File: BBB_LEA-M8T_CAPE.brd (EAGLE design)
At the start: 54.6 x 71.8 mm, 36 parts, among them U2 MIC5225-3.3

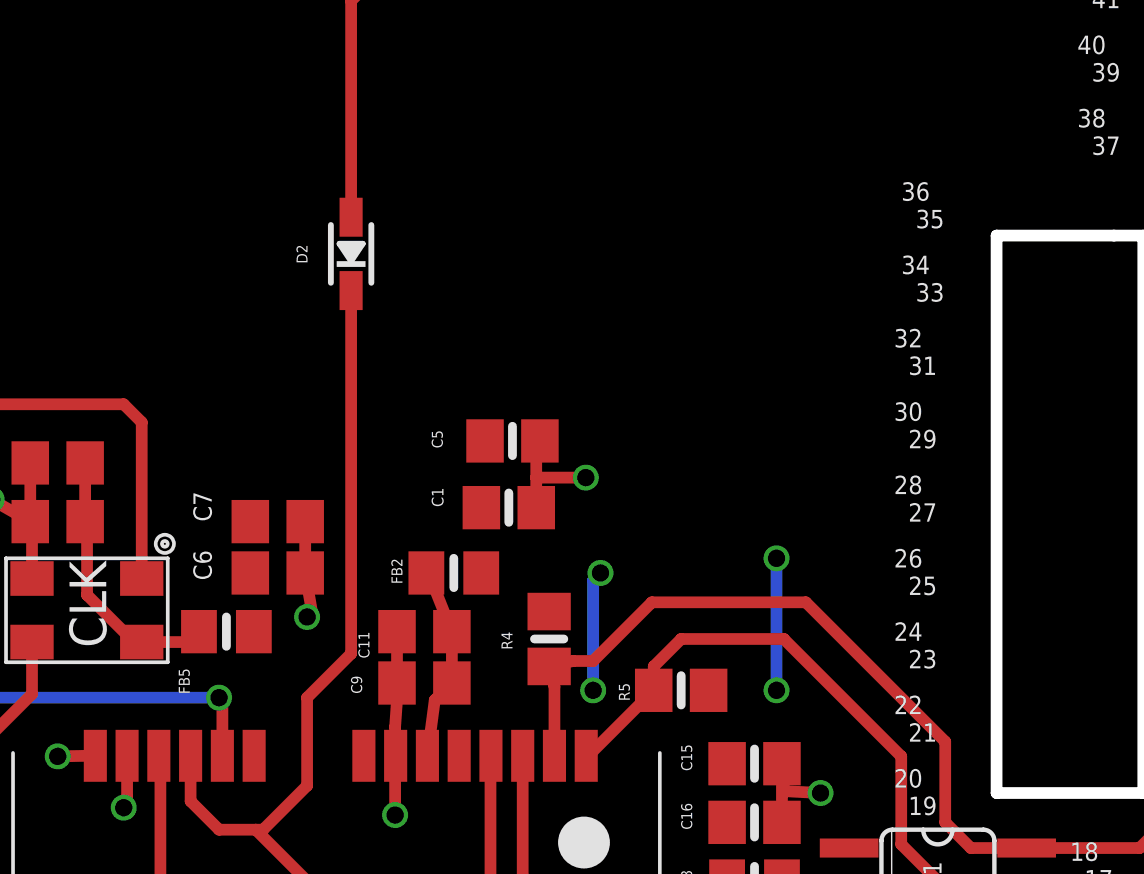
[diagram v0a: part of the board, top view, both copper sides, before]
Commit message: BOM updates associated with populating first test boards
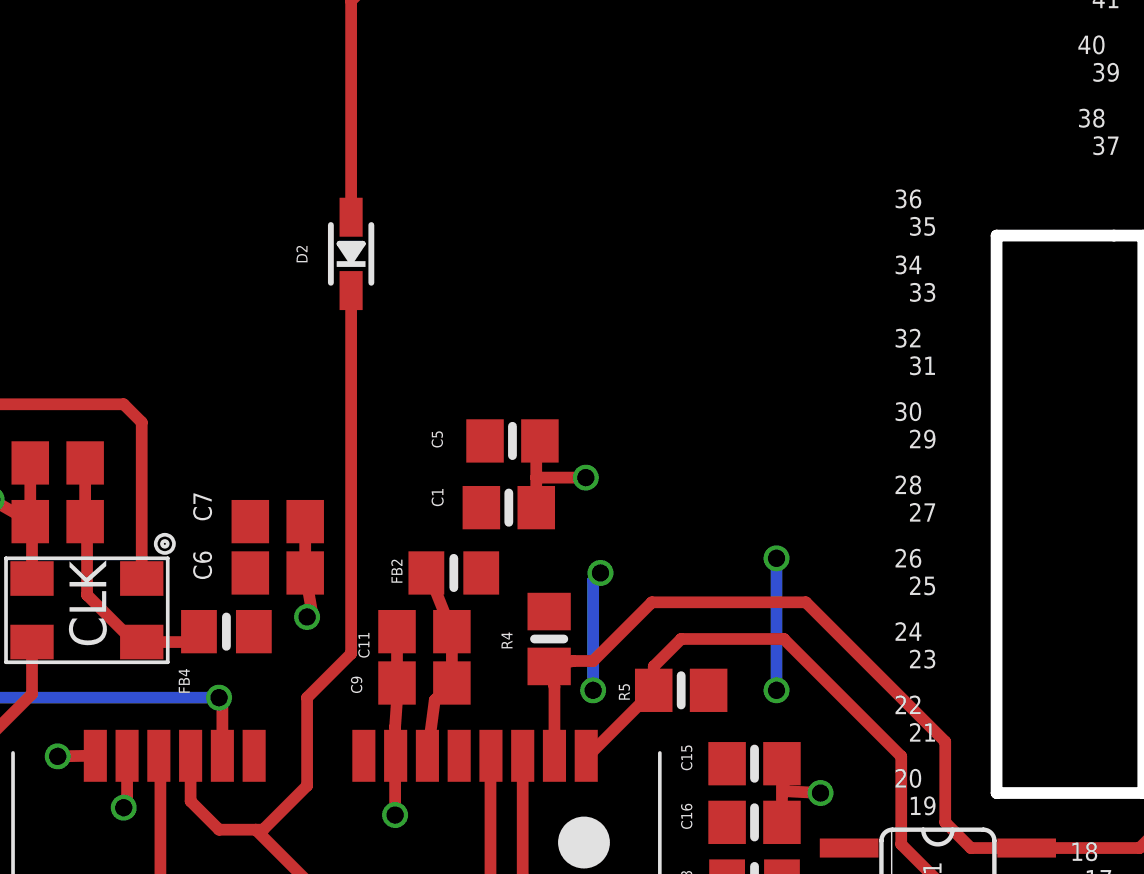
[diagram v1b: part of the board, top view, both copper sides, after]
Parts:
- C14, C7: value 22u -> 10u
- renumbered FB5 to FB4
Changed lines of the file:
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@@
 <text x="49.276" y="49.276" size="0.635" layer="25">38
   37</text>
-<text x="43.18" y="46.736" size="0.635" layer="25">36
+<text x="42.926" y="46.482" size="0.635" layer="25">36
   35</text>
-<text x="43.18" y="44.196" size="0.635" layer="25">34
+<text x="42.926" y="44.196" size="0.635" layer="25">34
   33</text>
 <text x="42.926" y="41.656" size="0.635" layer="25">32
@@
 <attribute name="NAME" x="19.304" y="34.544" size="0.635" layer="25" rot="R90"/>
 </element>
-<element name="C7" library="rcl" package="C0805" value="22u" x="21.59" y="36.576" smashed="yes">
+<element name="C7" library="rcl" package="C0805" value="10u" x="21.59" y="36.576" smashed="yes">
 <attribute name="NAME" x="19.304" y="36.576" size="0.635" layer="25" rot="R90"/>
 </element>
@@
 <attribute name="NAME" x="35.56" y="10.795" size="0.381" layer="25" ratio="18" rot="R180"/>
 </element>
-<element name="C14" library="rcl" package="C0805" value="22u" x="13.97" y="38.608" smashed="yes">
+<element name="C14" library="rcl" package="C0805" value="10u" x="13.97" y="38.608" smashed="yes">
 <attribute name="NAME" x="11.938" y="38.354" size="0.381" layer="25" rot="R90"/>
 </element>
-<element name="FB5" library="microbuilder" package="0805-NO@1" value="Ferrite" x="19.812" y="32.766" smashed="yes" rot="R180">
+<element name="FB4" library="microbuilder" package="0805-NO@1" value="Ferrite" x="19.812" y="32.766" smashed="yes" rot="R180">
 <attribute name="NAME" x="18.161" y="31.496" size="0.381" layer="25" ratio="18" rot="R270"/>
 </element>
@@
 <contactref element="C5" pad="1"/>
 <contactref element="C10" pad="1"/>
-<contactref element="FB5" pad="1"/>
+<contactref element="FB4" pad="1"/>
 <contactref element="C15" pad="1"/>
 <contactref element="C16" pad="1"/>
@@
 <contactref element="C4" pad="2"/>
 <contactref element="C14" pad="2"/>
-<contactref element="FB5" pad="2"/>
+<contactref element="FB4" pad="2"/>
 <wire x1="16.88" y1="32.406" x2="16.616" y2="32.406" width="0.4064" layer="1"/>
 <wire x1="16.616" y1="32.406" x2="14.986" y2="34.036" width="0.4064" layer="1"/>

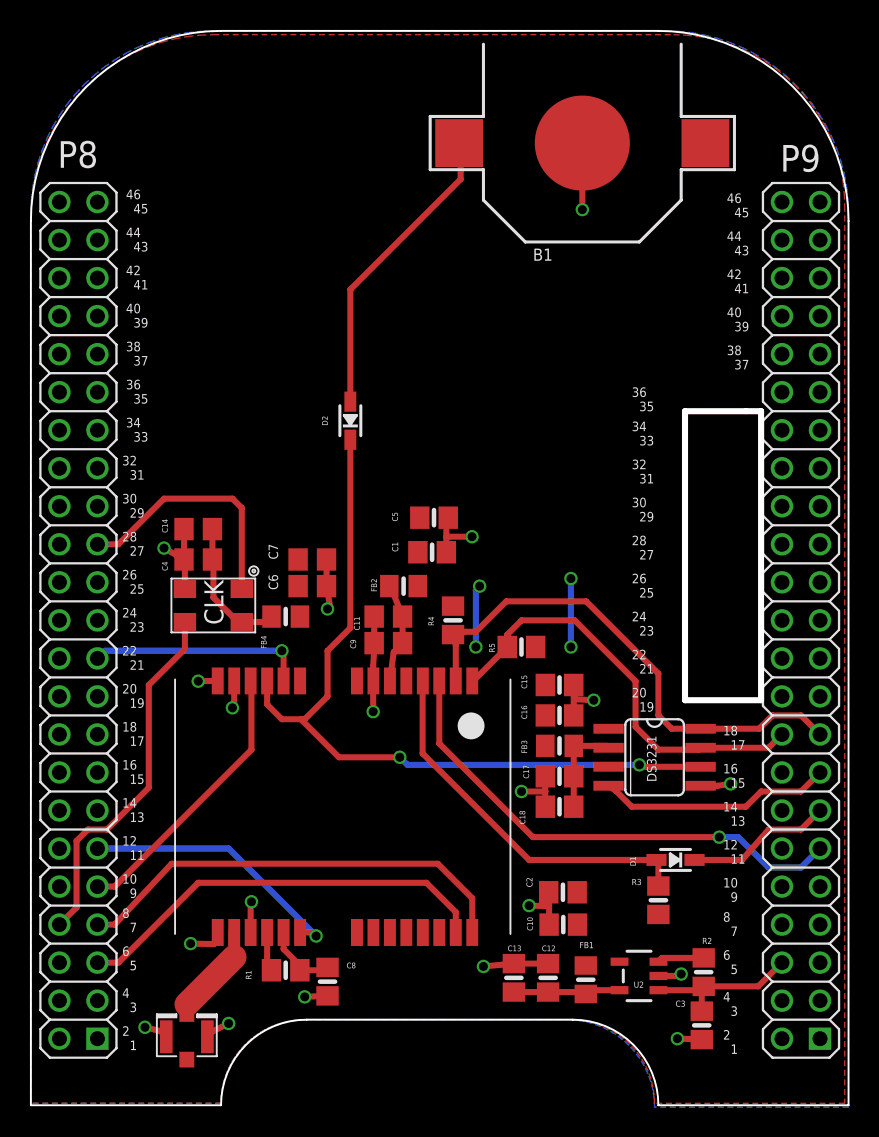
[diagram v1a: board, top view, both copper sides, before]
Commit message: minor updates to silkscreen layout to better match OSH Park silkscreen resolution
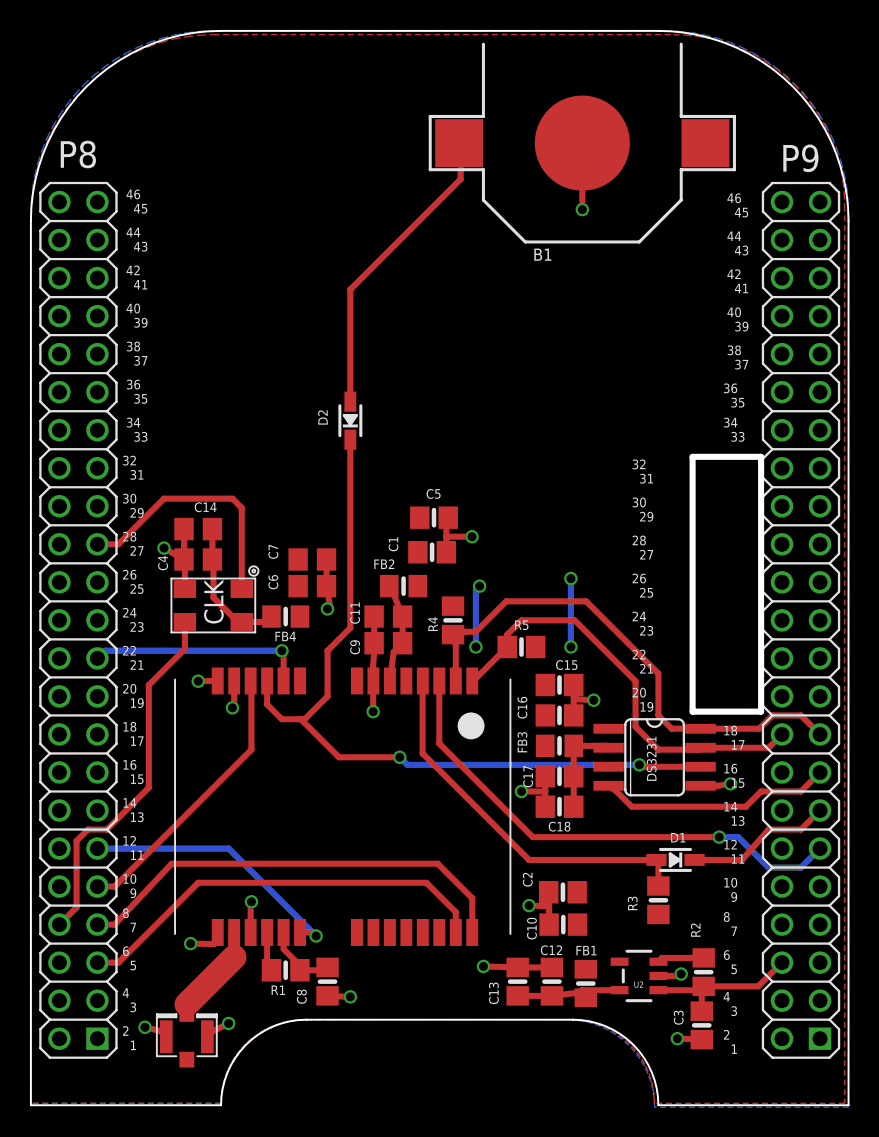
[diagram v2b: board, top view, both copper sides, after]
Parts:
- moved C12 0.36 mm to (37.6, 8.38)
- moved C13 0.36 mm to (35.3, 8.38)
- moved FB1 0.25 mm to (39.9, 8.26)
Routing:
- net GND: track 58.1 -> 58.8 mm

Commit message: minor layout and silkscreen cleanup
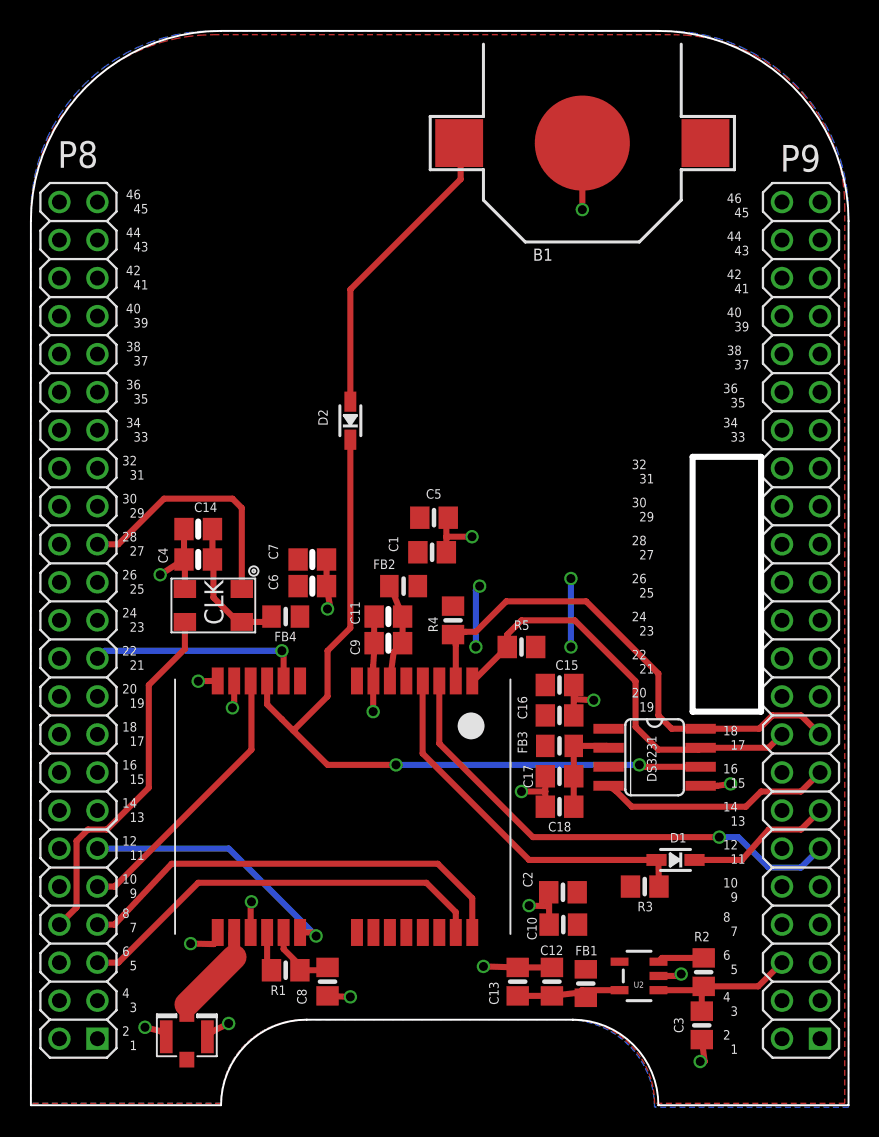
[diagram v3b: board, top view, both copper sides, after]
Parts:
- moved R3 1.29 mm to (43.8, 14.7), turned to 0 degrees
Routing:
- net VBACKUP: track 52.4 -> 53.2 mm
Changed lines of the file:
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@@
 <text x="49.022" y="6.096" size="0.635" layer="25">4
   3</text>
+<wire x1="13.97" y1="39.116" x2="13.97" y2="38.1" width="0.4064" layer="20"/>
+<wire x1="13.97" y1="37.084" x2="13.97" y2="36.068" width="0.4064" layer="20"/>
+<wire x1="21.59" y1="37.084" x2="21.59" y2="36.068" width="0.4064" layer="20"/>
+<wire x1="21.59" y1="35.306" x2="21.59" y2="34.29" width="0.4064" layer="20"/>
+<wire x1="26.67" y1="33.274" x2="26.67" y2="32.258" width="0.4064" layer="20"/>
+<wire x1="26.67" y1="31.496" x2="26.67" y2="30.48" width="0.4064" layer="20"/>
 </plain>
 <attributes>
@@
 </element>
 <element name="R2" library="microbuilder" package="0805-NO" value="10K" x="47.728" y="9.017" smashed="yes" rot="R270">
-<attribute name="NAME" x="47.522" y="11.303" size="0.635" layer="25" rot="R90"/>
+<attribute name="NAME" x="48.133" y="11.708" size="0.635" layer="25" rot="R180"/>
 </element>
 <element name="C2" library="microbuilder" package="0805-NO" value="10uF" x="38.33" y="14.351" smashed="yes" rot="R180">
@@
 </element>
 <element name="C3" library="microbuilder" package="0805-NO" value="10uF" x="47.601" y="5.461" smashed="yes" rot="R270">
-<attribute name="NAME" x="46.379" y="5.461" size="0.635" layer="25" rot="R90"/>
+<attribute name="NAME" x="46.379" y="4.953" size="0.635" layer="25" rot="R90"/>
 </element>
 <element name="D1" library="microbuilder" package="SOD-323" value="1N4148" x="45.847" y="16.51" smashed="yes" rot="R180">
 <attribute name="NAME" x="45.477" y="17.675" size="0.635" layer="25" font="vector"/>
 </element>
-<element name="R3" library="microbuilder" package="0805-NO" value="10K" x="44.704" y="13.819" smashed="yes" rot="R90">
-<attribute name="NAME" x="42.672" y="14.121" size="0.635" layer="25" rot="R270"/>
+<element name="R3" library="microbuilder" package="0805-NO" value="10K" x="43.791" y="14.732" smashed="yes">
+<attribute name="NAME" x="44.347" y="13.716" size="0.635" layer="25" rot="R180"/>
 </element>
 <element name="B1" library="microbuilder" package="CR1220" value="CR1220" x="39.624" y="64.389" smashed="yes">
@@
 <element name="U$3" library="tuckerLib" package="TAITIEN_TW-SERIES_OSCILLATOR" value="TAITIEN_TW-SERIES_OSCILLATOR" x="17.78" y="35.306" rot="R180"/>
 <element name="C4" library="rcl" package="C0805" value="0.1uf" x="13.97" y="36.576" smashed="yes">
-<attribute name="NAME" x="11.938" y="35.814" size="0.635" layer="25" rot="R90"/>
+<attribute name="NAME" x="11.938" y="36.322" size="0.635" layer="25" rot="R90"/>
 </element>
 <element name="C9" library="rcl" package="C0805" value="0.1uf" x="26.67" y="30.988" smashed="yes" rot="R180">
@@
 <contactref element="C12" pad="2"/>
 <contactref element="C14" pad="1"/>
-<via x="11.684" y="37.338" extent="1-16" drill="0.6" shape="square"/>
+<via x="11.43" y="35.56" extent="1-16" drill="0.6" shape="square"/>
 <wire x1="13.08" y1="34.606" x2="13.08" y2="36.516" width="0.4064" layer="1"/>
 <wire x1="13.08" y1="36.516" x2="13.02" y2="36.576" width="0.4064" layer="1"/>
 <wire x1="13.02" y1="36.576" x2="13.02" y2="38.608" width="0.4064" layer="1"/>
-<wire x1="13.02" y1="36.576" x2="11.684" y2="37.338" width="0.4064" layer="1"/>
+<wire x1="13.02" y1="36.576" x2="11.43" y2="35.56" width="0.4064" layer="1"/>
 <wire x1="22.54" y1="36.576" x2="22.54" y2="34.798" width="0.4064" layer="1"/>
 <via x="22.606" y="33.274" extent="1-16" drill="0.6" shape="square"/>
@@
 <wire x1="11.833" y1="4.699" x2="11.452" y2="5.08" width="0.4064" layer="1"/>
 <wire x1="11.452" y1="5.08" x2="10.414" y2="5.334" width="0.4064" layer="1"/>
-<via x="45.974" y="4.572" extent="1-16" drill="0.6" shape="square"/>
-<wire x1="45.974" y1="4.572" x2="46.27" y2="4.572" width="0.4064" layer="1"/>
-<wire x1="46.27" y1="4.572" x2="47.601" y2="4.511" width="0.4064" layer="1"/>
+<via x="47.498" y="3.048" extent="1-16" drill="0.6" shape="square"/>
+<wire x1="47.498" y1="3.048" x2="47.794" y2="3.048" width="0.4064" layer="1"/>
+<wire x1="47.794" y1="3.048" x2="47.601" y2="4.511" width="0.4064" layer="1"/>
 <via x="33.02" y="9.398" extent="1-16" drill="0.6" shape="square"/>
 <wire x1="33.02" y1="9.398" x2="35.306" y2="9.332" width="0.4064" layer="1"/>
@@
 <wire x1="18.572" y1="28.466" x2="18.572" y2="26.894" width="0.4064" layer="1"/>
 <wire x1="18.572" y1="26.894" x2="19.558" y2="25.908" width="0.4064" layer="1"/>
-<wire x1="19.558" y1="25.908" x2="20.828" y2="25.908" width="0.4064" layer="1"/>
-<wire x1="20.828" y1="25.908" x2="21.082" y2="25.908" width="0.4064" layer="1"/>
-<wire x1="21.082" y1="25.908" x2="22.606" y2="27.432" width="0.4064" layer="1"/>
+<wire x1="20.32" y1="25.146" x2="22.606" y2="27.432" width="0.4064" layer="1"/>
 <wire x1="22.606" y1="27.432" x2="22.606" y2="30.48" width="0.4064" layer="1"/>
 <wire x1="22.606" y1="30.48" x2="24.13" y2="32.004" width="0.4064" layer="1"/>
@@
 <wire x1="43.815" y1="22.733" x2="43.434" y2="22.86" width="0.4064" layer="1"/>
 <via x="43.434" y="22.86" extent="1-16" drill="0.6" shape="square"/>
-<via x="27.432" y="23.368" extent="1-16" drill="0.6" shape="square"/>
-<wire x1="27.432" y1="23.368" x2="23.368" y2="23.368" width="0.4064" layer="1"/>
-<wire x1="23.368" y1="23.368" x2="20.828" y2="25.908" width="0.4064" layer="1"/>
-<wire x1="27.432" y1="23.368" x2="27.94" y2="22.86" width="0.4064" layer="16"/>
-<wire x1="27.94" y1="22.86" x2="43.434" y2="22.86" width="0.4064" layer="16"/>
+<via x="27.178" y="22.86" extent="1-16" drill="0.6" shape="square"/>
+<wire x1="27.178" y1="22.86" x2="22.606" y2="22.86" width="0.4064" layer="1"/>
+<wire x1="22.606" y1="22.86" x2="20.32" y2="25.146" width="0.4064" layer="1"/>
+<wire x1="20.32" y1="25.146" x2="19.558" y2="25.908" width="0.4064" layer="1"/>
+<wire x1="27.178" y1="22.86" x2="43.434" y2="22.86" width="0.4064" layer="16"/>
 </signal>
 <signal name="TX">
@@
 <contactref element="D1" pad="A"/>
 <contactref element="U$1" pad="4"/>
-<wire x1="44.704" y1="14.769" x2="44.704" y2="16.383" width="0.4064" layer="1"/>
+<wire x1="44.741" y1="14.732" x2="44.704" y2="16.383" width="0.4064" layer="1"/>
 <wire x1="44.704" y1="16.383" x2="44.577" y2="16.51" width="0.4064" layer="1"/>
 <wire x1="44.577" y1="16.51" x2="36.068" y2="16.51" width="0.4064" layer="1"/>
